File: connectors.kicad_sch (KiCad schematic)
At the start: 13 parts

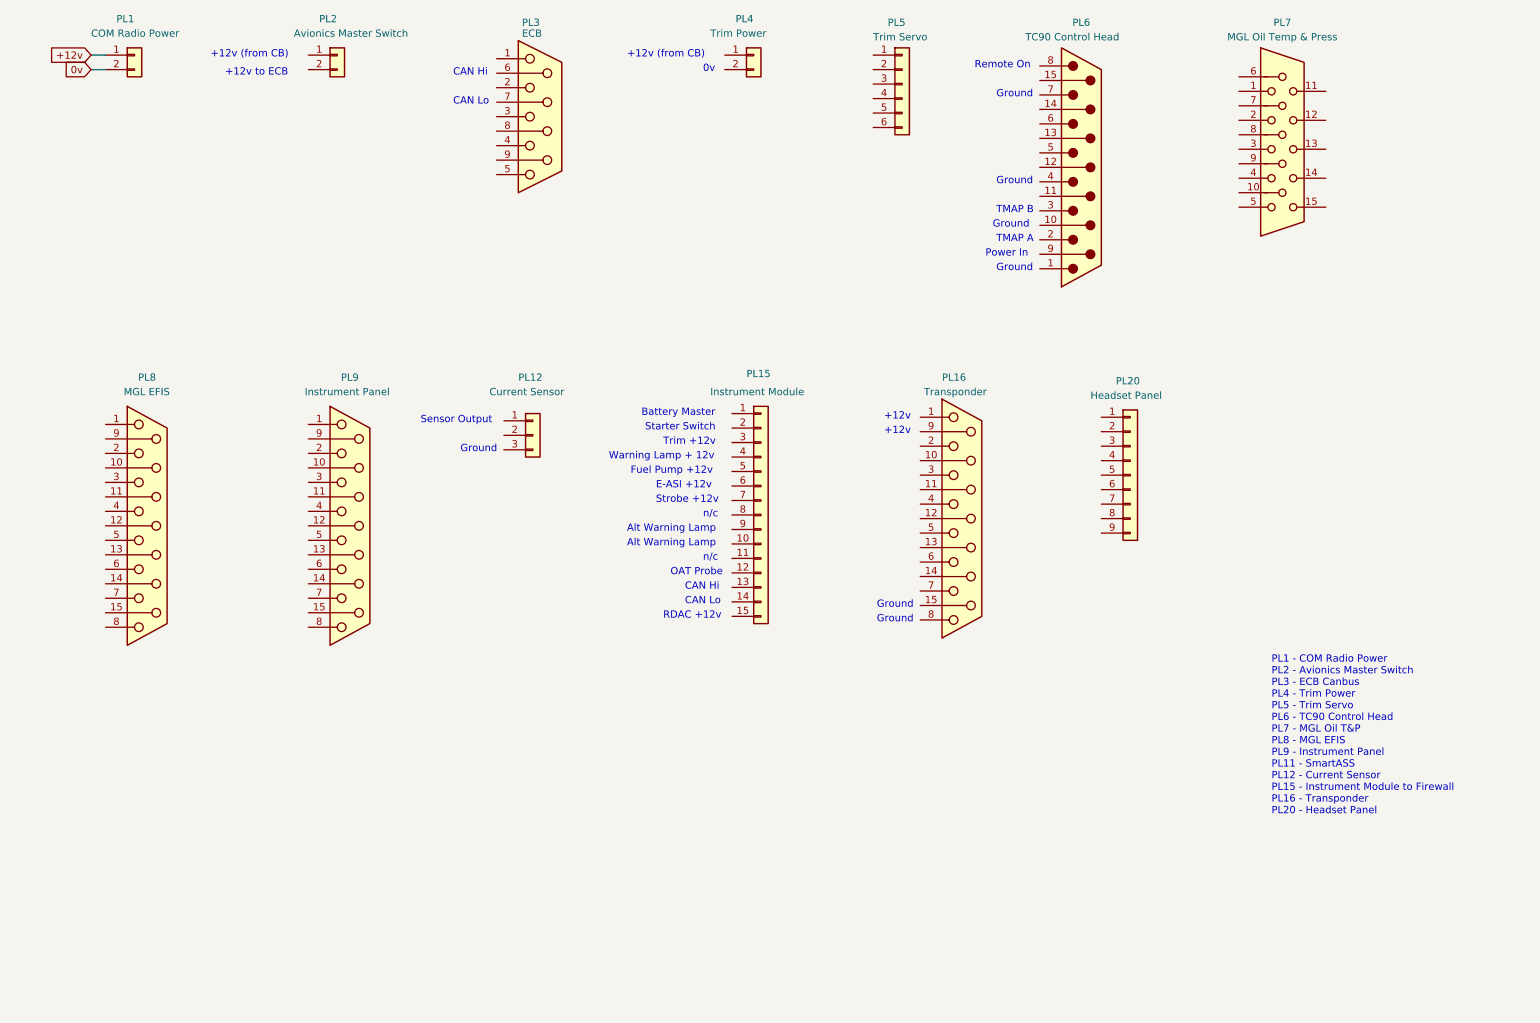
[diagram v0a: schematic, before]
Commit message: Completed content of Connectors sheet, started SmartAss sheet
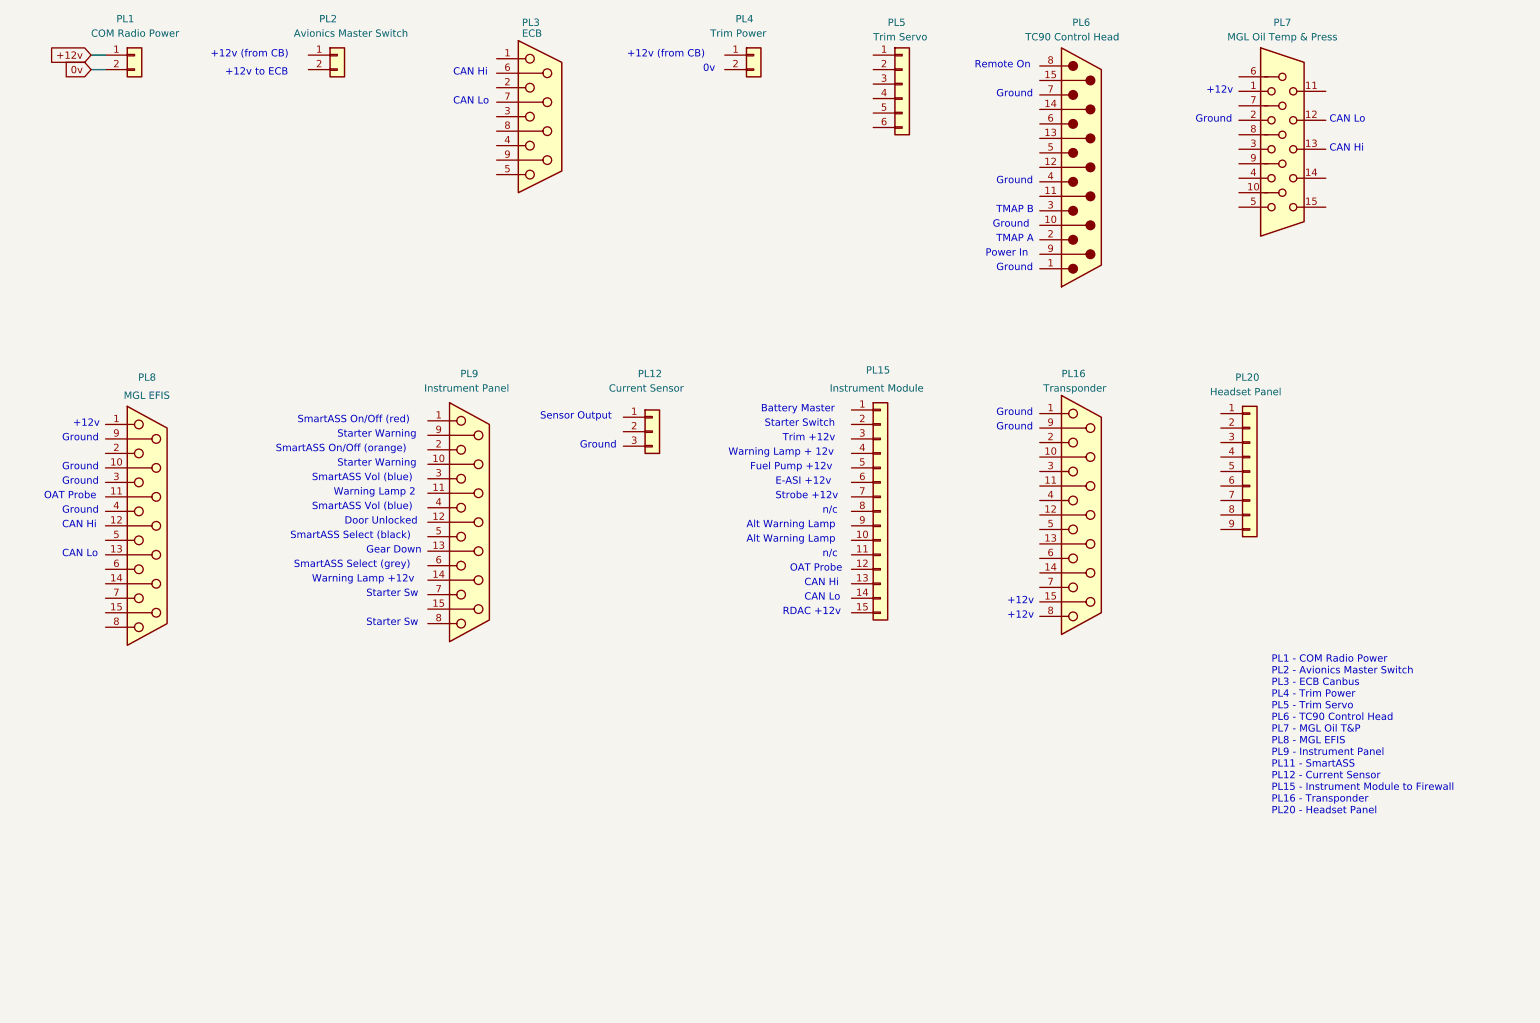
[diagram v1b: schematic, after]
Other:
- note added: "Door Unlocked"
- note added: "Gear Down"
- note added: "SmartASS On/Off (orange)"
- note added: "SmartASS On/Off (red)"
- note added: "SmartASS Select (black)"
- note added: "SmartASS Select (grey)"
- note added: "SmartASS Vol (blue)"
- note added: "Starter Sw"
- note added: "Starter Warning"
- note added: "Warning Lamp +12v"
- note added: "Warning Lamp 2"
- moved on the sheet: PL12, PL15, PL16, PL20, PL9

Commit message: Added PL20 to COM Sheet
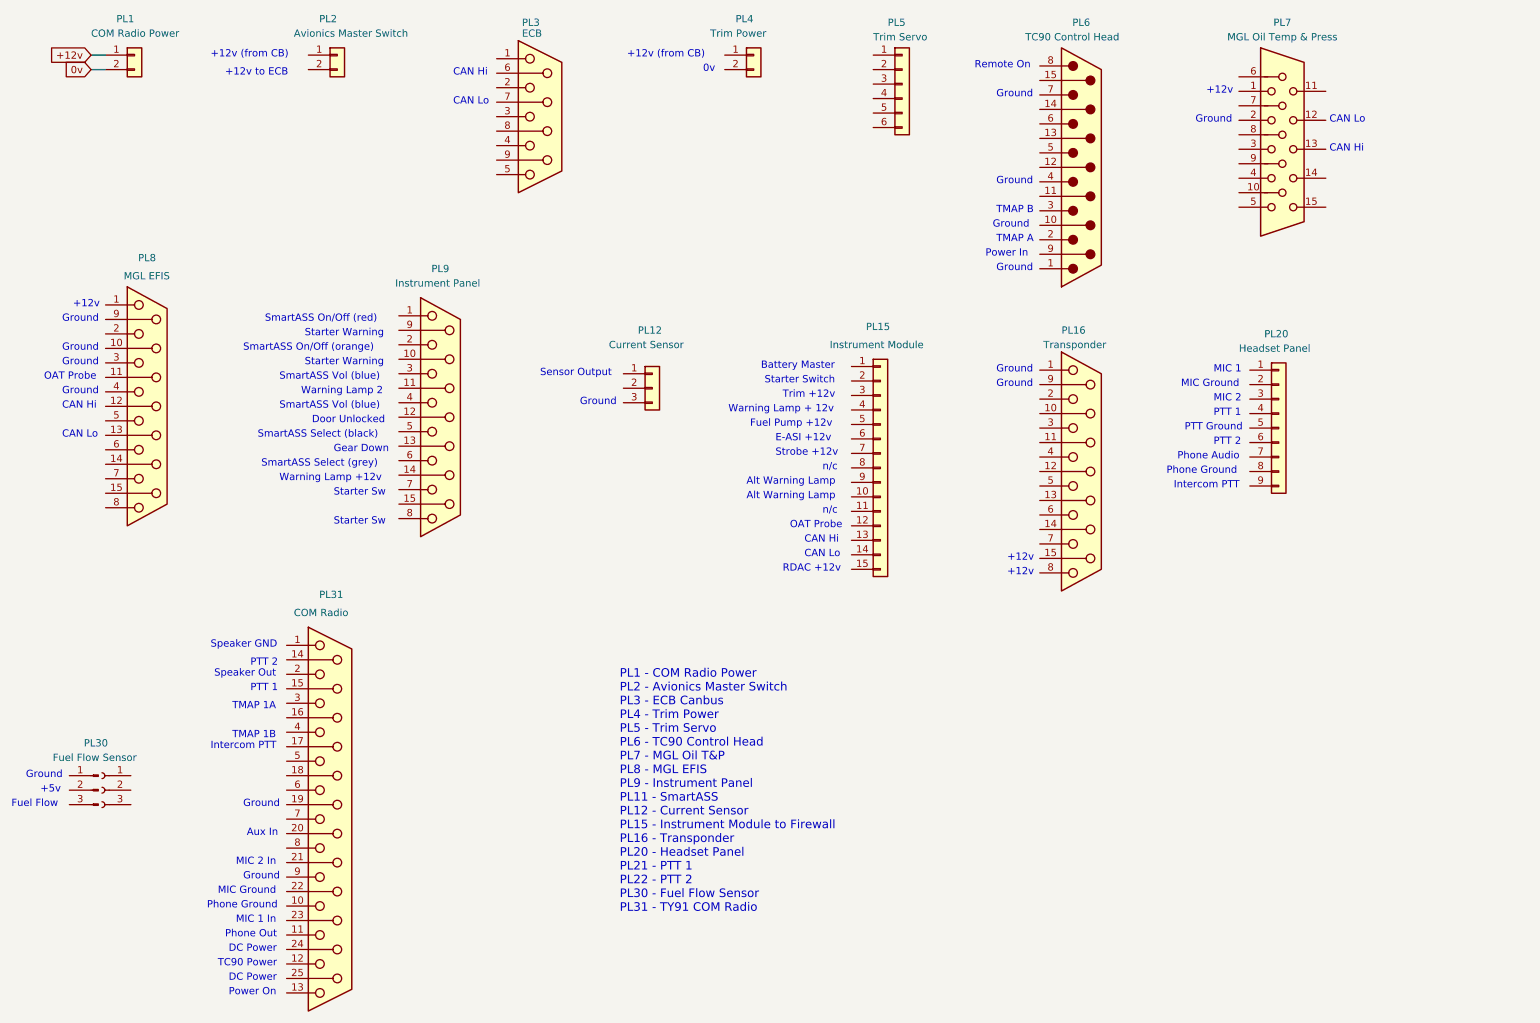
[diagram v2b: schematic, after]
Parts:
- added J?: Conn_01x03_Female, symbol Connector:Conn_01x03_Female
- added PL30: Fuel Flow Sensor, symbol Connector:Conn_01x03_Male
- added PL31: COM Radio, symbol Connector:DB25_Female
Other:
- note added: "+5v"
- note added: "Aux In"
- note added: "DC Power"
- note added: "Fuel Flow"
- note added: "Intercom PTT"
- note added: "MIC 1"
- note added: "MIC 1 In"
- note added: "MIC 2"
- note added: "MIC 2 In"
- note added: "MIC Ground"
- note added: "PL1 - COM Radio Power PL2 - Avionics Master Switch PL3 - ECB Canbus PL4 - Trim Power PL5 - Trim Servo PL6 - TC90 Control Head PL7 - MGL Oil T&P PL8 - MGL EFIS PL9 - Instrument Panel PL11 - SmartASS PL12 - Current Sensor PL15 - Instrument Module to Firewall PL16 - Transponder PL20 - Headset Panel PL21 - PTT 1 PL22 - PTT 2 PL30 - Fuel Flow Sensor PL31 - TY91 COM Radio"
- note added: "PTT 1"
- note added: "PTT 2"
- note added: "PTT Ground"
- note added: "Phone Audio"
- note added: "Phone Ground"
- note added: "Phone Out"
- note added: "Power On"
- note added: "Speaker GND"
- note added: "Speaker Out"
- note added: "TC90 Power"
- note added: "TMAP 1A"
- note added: "TMAP 1B"
- note removed: "PL1 - COM Radio Power PL2 - Avionics Master Switch PL3 - ECB Canbus PL4 - Trim Power PL5 - Trim Servo PL6 - TC90 Control Head PL7 - MGL Oil T&P PL8 - MGL EFIS PL9 - Instrument Panel PL11 - SmartASS PL12 - Current Sensor PL15 - Instrument Module to Firewall PL16 - Transponder PL20 - Headset Panel"
- moved on the sheet: PL12, PL15, PL16, PL20, PL8, PL9
